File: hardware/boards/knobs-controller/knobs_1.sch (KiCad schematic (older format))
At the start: 28 parts, among them J1 ZX62-AB-5PA(31), J4 JST---S4B-PH-SM4-TB(LF)(SN)_J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, J8 2X3_SMD_MALE, U3 ATSAMD21G18A-48, Y1 32.768KHz

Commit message: routed
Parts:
- removed D3: PMEG2005EL, knobs:MK1_ZERO_SODFL1008X40N-882D, symbol knobs-eagle-import:MK1_ZERO_PMEG2005EL
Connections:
- net labels added: VIN
- net labels removed: PA18_USB_ID, USB_ID
- wire segments 158 -> 152
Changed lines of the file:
@@
 Connection ~ 3100 7400
 Wire Wire Line
-	3400 3400 4400 3400
-Text Label 3600 3400 0    70   ~ 0
-PA18_USB_ID
-Wire Wire Line
-	1600 3400 3200 3400
-Text Label 2100 3400 0    70   ~ 0
-USB_ID
-Wire Wire Line
 	1600 3300 2700 3300
 Wire Wire Line
@@
 Wire Wire Line
 	2700 3900 2700 3300
-Wire Wire Line
-	2700 3100 2700 3300
 Connection ~ 2700 3300
 Text Label 3600 3300 0    70   ~ 0
@@
 Wire Wire Line
 	2600 3800 2600 3200
-Wire Wire Line
-	2600 2900 2600 3200
 Connection ~ 2600 3200
 Text Label 3600 3200 0    70   ~ 0
@@
 Wire Wire Line
 	3700 2300 4100 2300
-Wire Wire Line
-	4100 2300 4100 2200
 Connection ~ 3700 2300
 Text GLabel 3600 2300 0    10   BiDi ~ 0
-VUSB
-Wire Wire Line
-	14700 7200 15200 7200
-Text GLabel 15200 7200 2    70   BiDi ~ 0
 VUSB
 Wire Wire Line
@@
 $EndComp
 $Comp
-L knobs-eagle-import:MK1_ZERO_PMEG2005EL D3
-U 1 1 16D8F47B
-P 3300 3400
-AR Path="/16D8F47B" Ref="D3"  Part="1"
-AR Path="/5D86641C/16D8F47B" Ref="D3"  Part="1"
-F 0 "D3" H 3201 3390 59  0000 R TNN
-F 1 "PMEG2005EL" H 3290 3485 59  0000 C BNN
-F 2 "knobs:MK1_ZERO_SODFL1008X40N-882D" H 3300 3400 50  0001 C CNN
-F 3 "" H 3300 3400 50  0001 C CNN
-	1    3300 3400
-	-1   0    0    1
-$EndComp
-$Comp
 L knobs-eagle-import:RESISTOR-NICK_C-EUC0805 C6
 U 1 1 7C2E67B4
@@
 F 3 "" H 7450 4800 50  0001 C CNN
 	1    7450 4800
-	1    0    0    -1
-$EndComp
-$Comp
-L knobs-eagle-import:JST---S4B-PH-SM4-TB(LF)(SN)_JST_S4B-PH-SM4-TB_LF_SNJST_S4B-PH-SM4-TB_LF_SN_0_0 J4
-U 1 1 5FA14143
-P 13900 6200
-AR Path="/5FA14143" Ref="J4"  Part="1"
-AR Path="/5D86641C/5FA14143" Ref="J4"  Part="1"
-F 0 "J4" H 14000 6100 85  0000 L TNN
-F 1 "JST---S4B-PH-SM4-TB(LF)(SN)_JST_S4B-PH-SM4-TB_LF_SNJST_S4B-PH-SM4-TB_LF_SN_0_0" H 13900 6200 50  0001 C CNN
-F 2 "knobs:JST---S4B-PH-SM4-TB(LF)(SN)_JST_S4B-PH-SM4-TB_LF_SN_0" H 13900 6200 50  0001 C CNN
-F 3 "" H 13900 6200 50  0001 C CNN
-	1    13900 6200
 	1    0    0    -1
 $EndComp
@@
 Connection ~ 8900 9600
 $Comp
-L power:+3V3 #PWR?
+L power:+3V3 #PWR0101
 U 1 1 5D8E291C
 P 12950 4700
-F 0 "#PWR?" H 12950 4550 50  0001 C CNN
+F 0 "#PWR0101" H 12950 4550 50  0001 C CNN
 F 1 "+3V3" H 12965 4873 50  0000 C CNN
 F 2 "" H 12950 4700 50  0001 C CNN
@@
 $EndComp
 $Comp
-L power:+3V3 #PWR?
+L power:+3V3 #PWR0102
 U 1 1 5D8E3846
 P 12950 3600
-F 0 "#PWR?" H 12950 3450 50  0001 C CNN
+F 0 "#PWR0102" H 12950 3450 50  0001 C CNN
 F 1 "+3V3" H 12965 3773 50  0000 C CNN
 F 2 "" H 12950 3600 50  0001 C CNN
@@
 $EndComp
 $Comp
-L power:+3V3 #PWR?
+L power:+3V3 #PWR0103
 U 1 1 5D8F80D5
 P 12950 2450
-F 0 "#PWR?" H 12950 2300 50  0001 C CNN
+F 0 "#PWR0103" H 12950 2300 50  0001 C CNN
 F 1 "+3V3" H 12965 2623 50  0000 C CNN
 F 2 "" H 12950 2450 50  0001 C CNN
@@
 $EndComp
 $Comp
-L power:+3V3 #PWR?
+L power:+3V3 #PWR0104
 U 1 1 5D8F9A02
 P 12950 1250
-F 0 "#PWR?" H 12950 1100 50  0001 C CNN
+F 0 "#PWR0104" H 12950 1100 50  0001 C CNN
 F 1 "+3V3" H 12965 1423 50  0000 C CNN
 F 2 "" H 12950 1250 50  0001 C CNN
@@
 $EndComp
 $Comp
-L power:GND #PWR?
+L power:GND #PWR0105
 U 1 1 5D905290
 P 12950 1850
-F 0 "#PWR?" H 12950 1600 50  0001 C CNN
+F 0 "#PWR0105" H 12950 1600 50  0001 C CNN
 F 1 "GND" H 12955 1677 50  0000 C CNN
 F 2 "" H 12950 1850 50  0001 C CNN
@@
 $EndComp
 $Comp
-L power:GND #PWR?
+L power:GND #PWR0106
 U 1 1 5D90F9A2
 P 12950 3050
-F 0 "#PWR?" H 12950 2800 50  0001 C CNN
+F 0 "#PWR0106" H 12950 2800 50  0001 C CNN
 F 1 "GND" H 12955 2877 50  0000 C CNN
 F 2 "" H 12950 3050 50  0001 C CNN
@@
 $EndComp
 $Comp
-L power:GND #PWR?
+L power:GND #PWR0107
 U 1 1 5D90FDB0
 P 12950 4200
-F 0 "#PWR?" H 12950 3950 50  0001 C CNN
+F 0 "#PWR0107" H 12950 3950 50  0001 C CNN
 F 1 "GND" H 12955 4027 50  0000 C CNN
 F 2 "" H 12950 4200 50  0001 C CNN
@@
 $EndComp
 $Comp
-L power:GND #PWR?
+L power:GND #PWR0108
 U 1 1 5D9104CC
 P 12950 5300
-F 0 "#PWR?" H 12950 5050 50  0001 C CNN
+F 0 "#PWR0108" H 12950 5050 50  0001 C CNN
 F 1 "GND" H 12955 5127 50  0000 C CNN
 F 2 "" H 12950 5300 50  0001 C CNN
@@
 	6400 4800 7250 4800
 $Comp
-L power:GND #PWR?
+L power:GND #PWR0109
 U 1 1 5DAA89E9
 P 7750 5100
-F 0 "#PWR?" H 7750 4850 50  0001 C CNN
+F 0 "#PWR0109" H 7750 4850 50  0001 C CNN
 F 1 "GND" H 7755 4927 50  0000 C CNN
 F 2 "" H 7750 5100 50  0001 C CNN
@@
 $EndComp
 $Comp
-L power:GND #PWR?
+L power:GND #PWR0110
 U 1 1 5DAAA24A
 P 2700 5900
-F 0 "#PWR?" H 2700 5650 50  0001 C CNN
+F 0 "#PWR0110" H 2700 5650 50  0001 C CNN
 F 1 "GND" H 2705 5727 50  0000 C CNN
 F 2 "" H 2700 5900 50  0001 C CNN
@@
 $EndComp
 $Comp
-L power:GND #PWR?
+L power:GND #PWR0111
 U 1 1 5DAAAB5A
 P 1800 4700
-F 0 "#PWR?" H 1800 4450 50  0001 C CNN
+F 0 "#PWR0111" H 1800 4450 50  0001 C CNN
 F 1 "GND" H 1805 4527 50  0000 C CNN
 F 2 "" H 1800 4700 50  0001 C CNN
@@
 $EndComp
 $Comp
-L power:GND #PWR?
+L power:GND #PWR0112
 U 1 1 5DAAB18E
 P 1400 4700
-F 0 "#PWR?" H 1400 4450 50  0001 C CNN
+F 0 "#PWR0112" H 1400 4450 50  0001 C CNN
 F 1 "GND" H 1405 4527 50  0000 C CNN
 F 2 "" H 1400 4700 50  0001 C CNN
@@
 $EndComp
 $Comp
-L power:GND #PWR?
+L power:GND #PWR0113
 U 1 1 5DAC5F05
 P 11800 9200
-F 0 "#PWR?" H 11800 8950 50  0001 C CNN
+F 0 "#PWR0113" H 11800 8950 50  0001 C CNN
 F 1 "GND" H 11805 9027 50  0000 C CNN
 F 2 "" H 11800 9200 50  0001 C CNN
@@
 $EndComp
 $Comp
-L power:+3V3 #PWR?
-U 1 1 5DAC8342
-P 12800 7900
-F 0 "#PWR?" H 12800 7750 50  0001 C CNN
-F 1 "+3V3" H 12815 8073 50  0000 C CNN
-F 2 "" H 12800 7900 50  0001 C CNN
-F 3 "" H 12800 7900 50  0001 C CNN
-	1    12800 7900
-	1    0    0    -1
-$EndComp
-Wire Wire Line
-	11700 7900 12800 7900
-$Comp
-L power:GND #PWR?
+L power:GND #PWR0114
 U 1 1 5DAD4C6A
 P 15700 6600
-F 0 "#PWR?" H 15700 6350 50  0001 C CNN
+F 0 "#PWR0114" H 15700 6350 50  0001 C CNN
 F 1 "GND" H 15705 6427 50  0000 C CNN
 F 2 "" H 15700 6600 50  0001 C CNN
@@
 	1    0    0    -1
 $EndComp
-Wire Bus Line
-	13800 8200 13800 9600
-Wire Bus Line
-	8900 7750 8900 9600
-Wire Bus Line
-	7800 7200 7800 9600
 $Comp
 L knobs-eagle-import:MK1_ZERO_BLM18PG471SN1D L2
@@
 	1    0    0    -1
 $EndComp
-$Comp
-L knobs-eagle-import:+3V3 #+3V?
-U 1 1 5D890552
-P 4100 2100
-AR Path="/5D890552" Ref="#+3V?"  Part="1"
-AR Path="/5D86641C/5D890552" Ref="#+3V?"  Part="1"
-F 0 "#+3V?" H 4100 2100 50  0001 C CNN
-F 1 "+3V3" H 4100 2120 59  0000 C BNN
-F 2 "" H 4100 2100 50  0001 C CNN
-F 3 "" H 4100 2100 50  0001 C CNN
-	1    4100 2100
-	1    0    0    -1
-$EndComp
+Text GLabel 4100 2300 2    59   Input ~ 0
+VIN
+$Comp
+L knobs-eagle-import:JST---S4B-PH-SM4-TB(LF)(SN)_JST_S4B-PH-SM4-TB_LF_SNJST_S4B-PH-SM4-TB_LF_SN_0_0 J4
+U 1 1 5FA14143
+P 13900 6200
+AR Path="/5FA14143" Ref="J4"  Part="1"
+AR Path="/5D86641C/5FA14143" Ref="J4"  Part="1"
+F 0 "J4" H 14000 6100 85  0000 L TNN
+F 1 "JST---S4B-PH-SM4-TB(LF)(SN)_JST_S4B-PH-SM4-TB_LF_SNJST_S4B-PH-SM4-TB_LF_SN_0_0" H 13900 6200 50  0001 C CNN
+F 2 "knobs:JST---S4B-PH-SM4-TB(LF)(SN)_JST_S4B-PH-SM4-TB_LF_SN_0" H 13900 6200 50  0001 C CNN
+F 3 "" H 13900 6200 50  0001 C CNN
+	1    13900 6200
+	1    0    0    -1
+$EndComp
+Wire Wire Line
+	14700 7200 15700 7200
+Wire Bus Line
+	13800 8200 13800 9600
+Wire Bus Line
+	8900 7750 8900 9600
+Wire Bus Line
+	7800 7200 7800 9600
+Text GLabel 15700 7200 2    59   Input ~ 0
+VIN
 $EndSCHEMATC

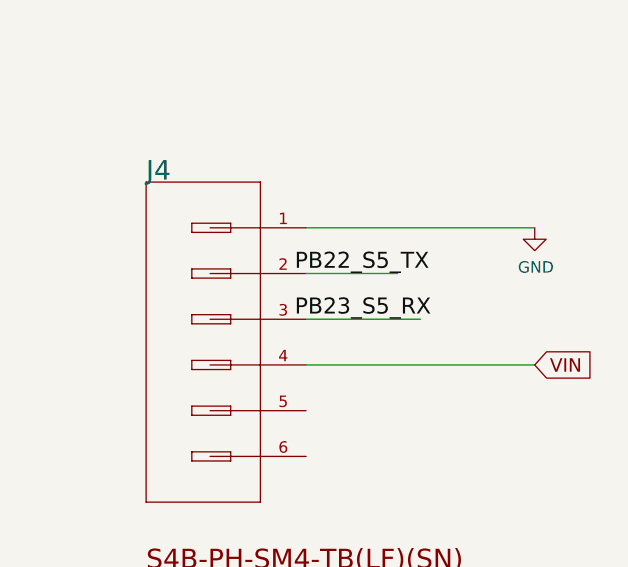
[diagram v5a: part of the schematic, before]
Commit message: correction: tx, rx connected
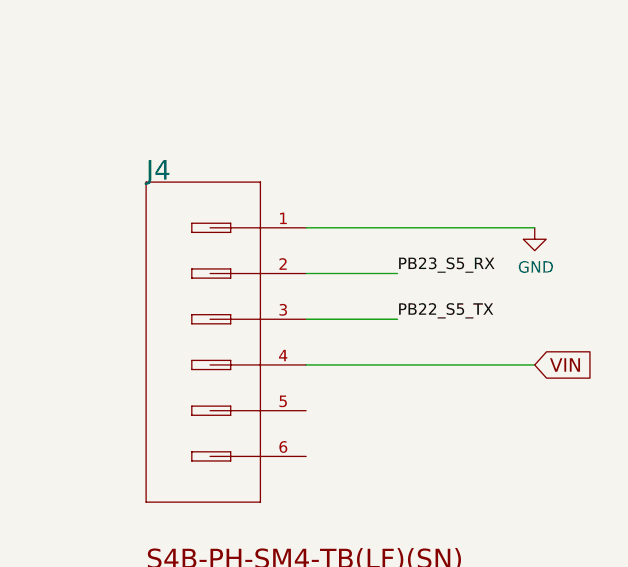
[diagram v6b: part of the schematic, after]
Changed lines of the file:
@@
-EESchema Schematic File Version 4
-LIBS:knobs-cache
+EESchema Schematic File Version 5
 EELAYER 30 0
 EELAYER END
@@
 Comment3 ""
 Comment4 ""
+Comment5 ""
+Comment6 ""
+Comment7 ""
+Comment8 ""
+Comment9 ""
 $EndDescr
 Wire Bus Line
@@
 PB23_S5_RX
 Wire Wire Line
-	14700 7000 15200 7000
-Text Label 14650 7000 0    70   ~ 0
-PB23_S5_RX
-Wire Wire Line
 	11700 8100 13700 8100
 Text Label 12700 8100 0    70   ~ 0
@@
 	7700 9300 6400 9300
 Text Label 6400 9300 0    70   ~ 0
-PB22_S5_TX
-Wire Wire Line
-	14700 6800 15100 6800
-Text Label 14650 6800 0    70   ~ 0
 PB22_S5_TX
 Wire Wire Line
@@
 Text GLabel 4100 2300 2    59   Input ~ 0
 VIN
+Wire Wire Line
+	14700 7200 15700 7200
+Text GLabel 15700 7200 2    59   Input ~ 0
+VIN
+Wire Wire Line
+	14700 6800 15100 6800
 $Comp
 L knobs-eagle-import:JST---S4B-PH-SM4-TB(LF)(SN)_JST_S4B-PH-SM4-TB_LF_SNJST_S4B-PH-SM4-TB_LF_SN_0_0 J4
@@
 $EndComp
 Wire Wire Line
-	14700 7200 15700 7200
+	14700 7000 15100 7000
+Text Label 15100 7000 0    50   ~ 0
+PB22_S5_TX
+Text Label 15100 6800 0    50   ~ 0
+PB23_S5_RX
 Wire Bus Line
 	13800 8200 13800 9600
@@
 Wire Bus Line
 	7800 7200 7800 9600
-Text GLabel 15700 7200 2    59   Input ~ 0
-VIN
 $EndSCHEMATC

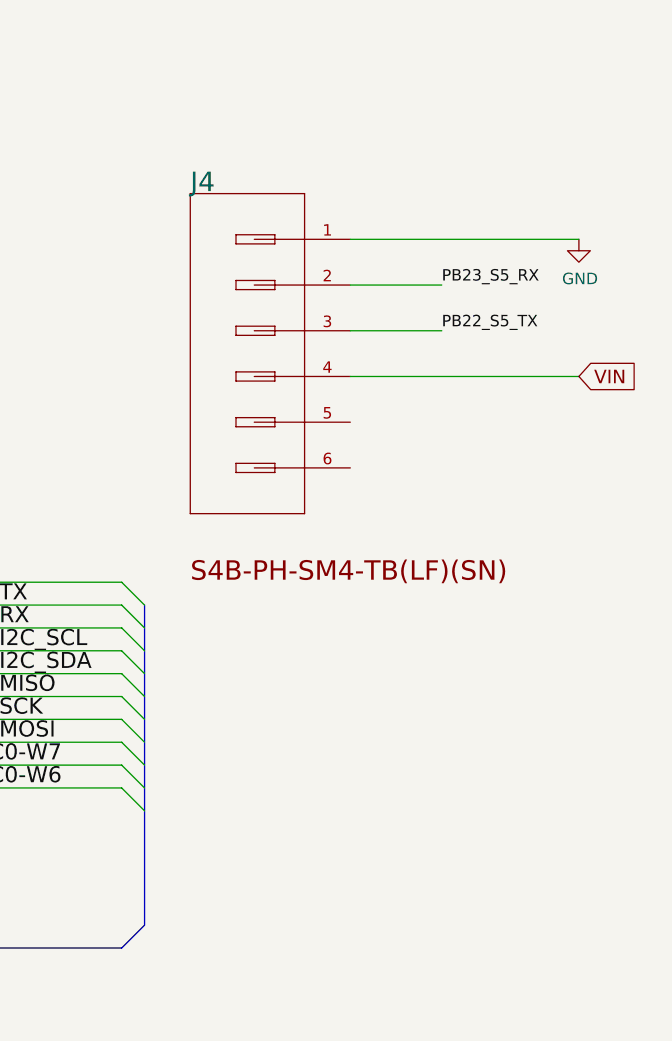
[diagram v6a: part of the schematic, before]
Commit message: v1.7: merge knobs and top breakout in to single board, remove fpc connector, replace with standard 0.1' pin header
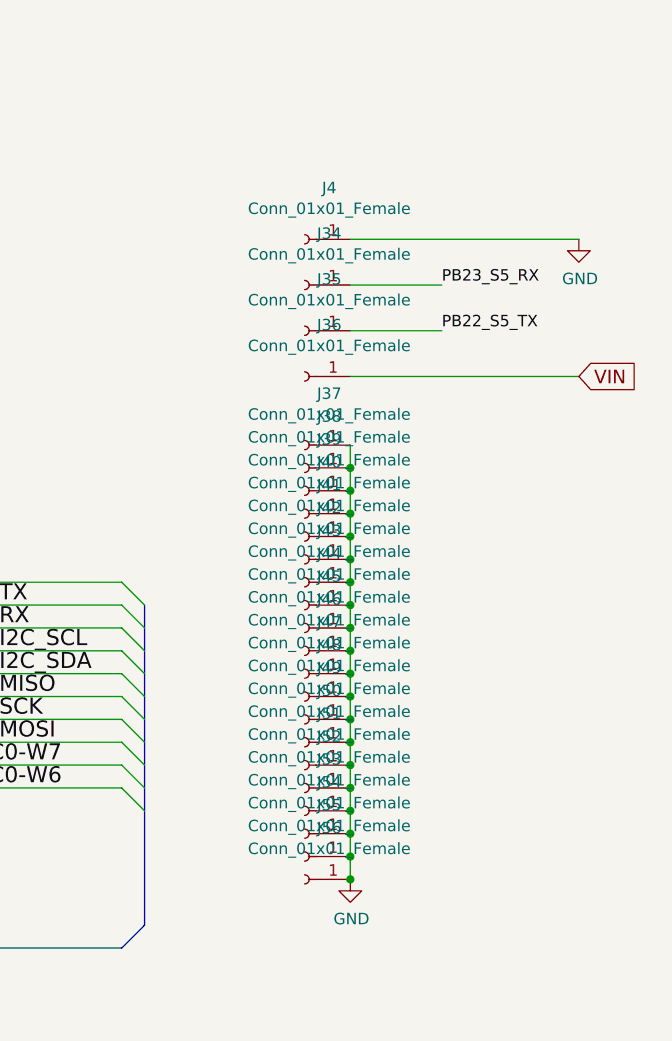
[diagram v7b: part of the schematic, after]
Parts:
- removed J4: JST---S4B-PH-SM4-TB(LF)(SN)_JST_S4B-PH-SM4-TB_LF_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, knobs:JST---S4B-PH-SM4-TB(LF)(SN)_JST_S4B-PH-SM4-TB_LF_SN_0, symbol knobs-eagle-import:JST---S4B-PH-SM4-TB(LF)(SN)_JST_S4B-PH-SM4-TB_LF_SNJST_S4B-P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
- added J34, J35, J36, J37, J38, J39, J4, J40, J41, J42, J43, J44, J45, J46, J47, J48, J49, J50, J51, J52, J53, J54, J55, J56: Conn_01x01_Female, Connector_PinSocket_2.54mm:PinSocket_1x01_P2.54mm_Vertical, symbol Connector:Conn_01x01_Female
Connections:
- wire segments 152 -> 171
